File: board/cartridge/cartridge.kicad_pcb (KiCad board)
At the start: 4 copper layers, 58.4 x 56 mm, 42 parts, among them J1 TF-115-BCP9, J2 HC-TYPE-C-16P-01B, P1 Card Edge, SW1 K3-1410S, SW2 K3-1410S, U1 AMS1117-3.3, U2 ESP32-S3-WROOM-1U, U3 TUSB320, U4 TXS0108E, U5 74LVC245, U6 74LVT14, U7 74LVC541, U8 74LVC541, U9 PCM5100

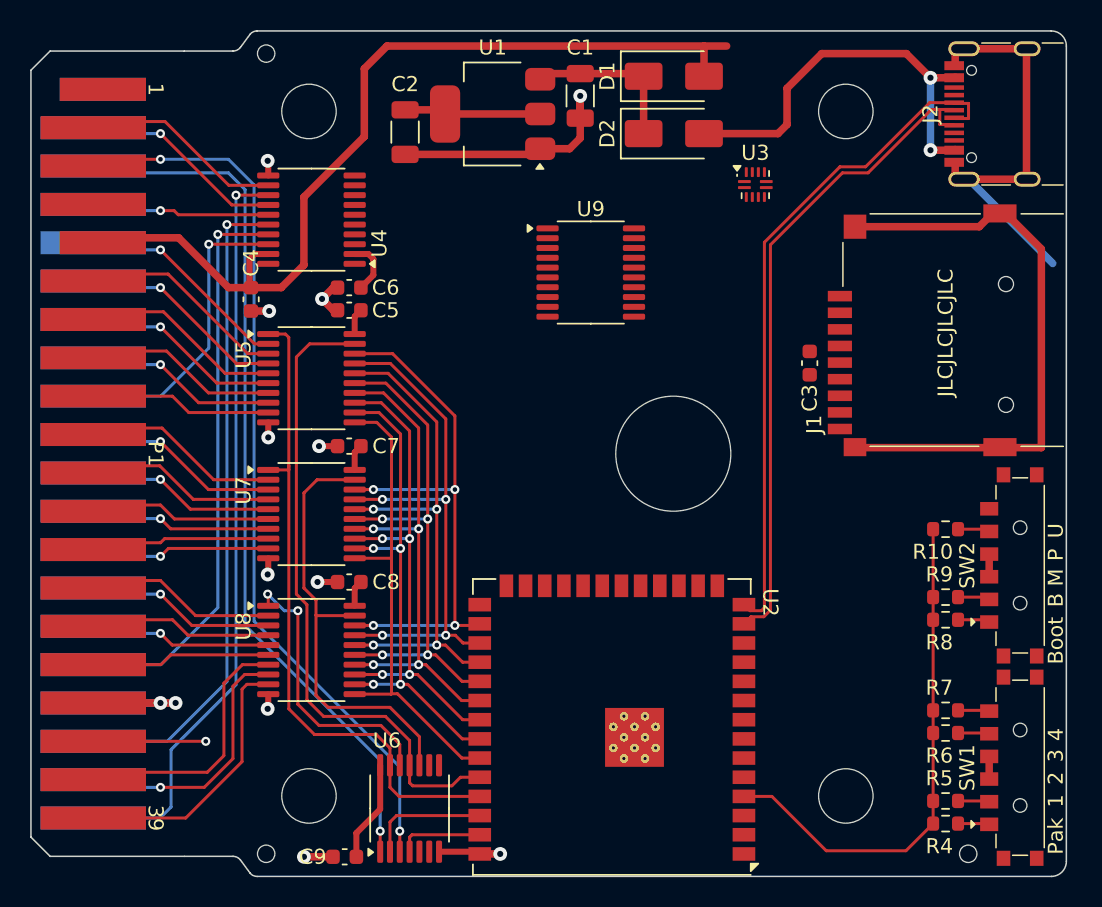
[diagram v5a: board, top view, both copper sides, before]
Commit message: Fully route 5V signals.
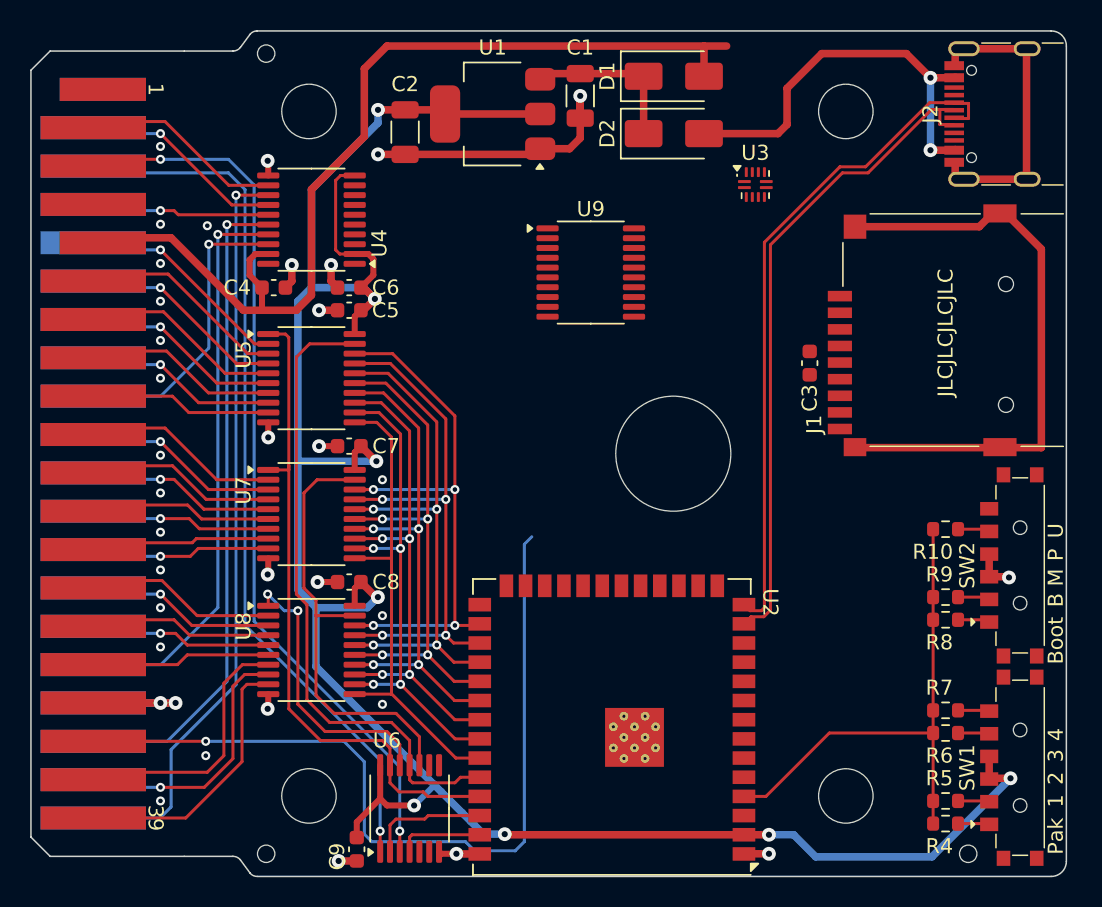
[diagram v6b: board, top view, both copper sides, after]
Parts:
- moved C4 1.69 mm to (127.5, 89.0), turned to 0 degrees
- moved C9 0.94 mm to (133.0, 126.2), turned to -90 degrees
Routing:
- net +3V3: track 26.1 -> 152.5 mm, vias 0 -> 8
- net /Host/SND: track 7.45 -> 55.0 mm
- net +5V: track 60.0 -> 64.5 mm
- net GND: track 112.6 -> 108.8 mm, vias 13 -> 35

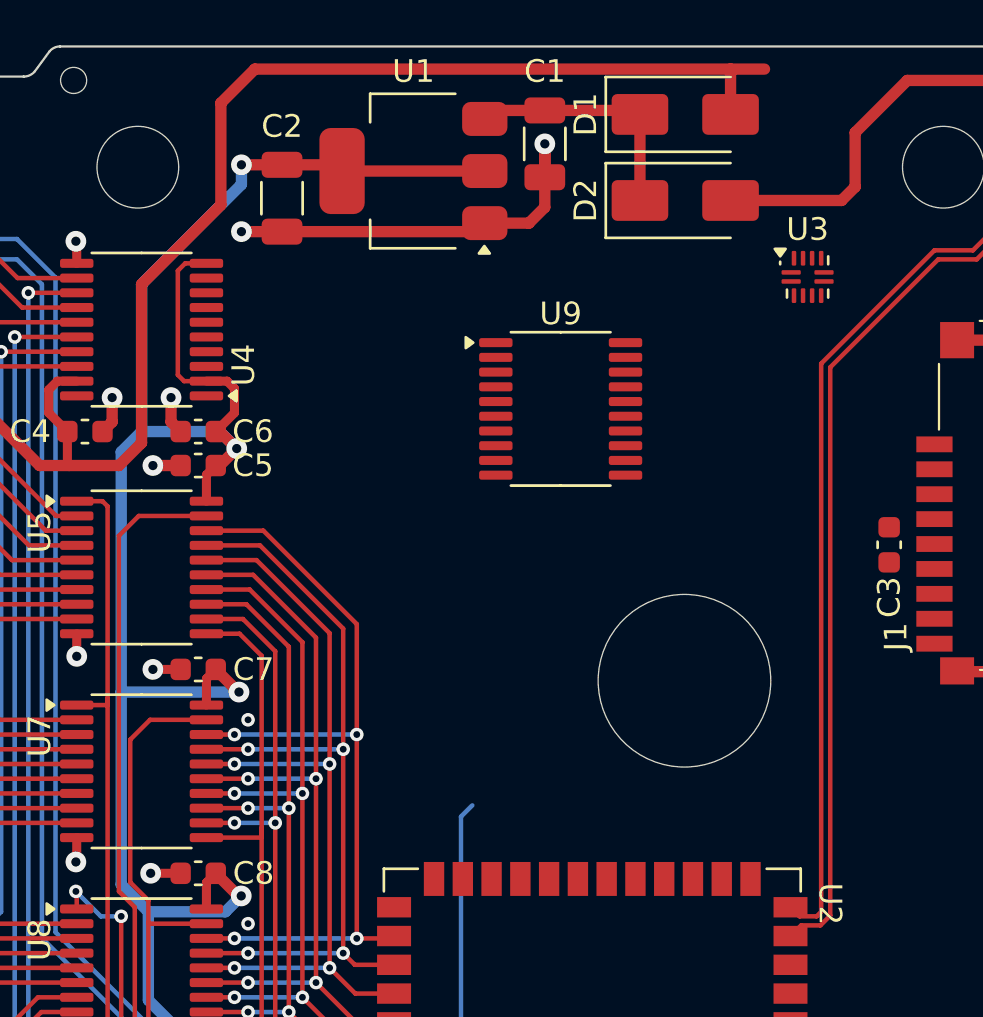
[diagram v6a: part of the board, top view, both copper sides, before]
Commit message: Attach control bus to MCU.
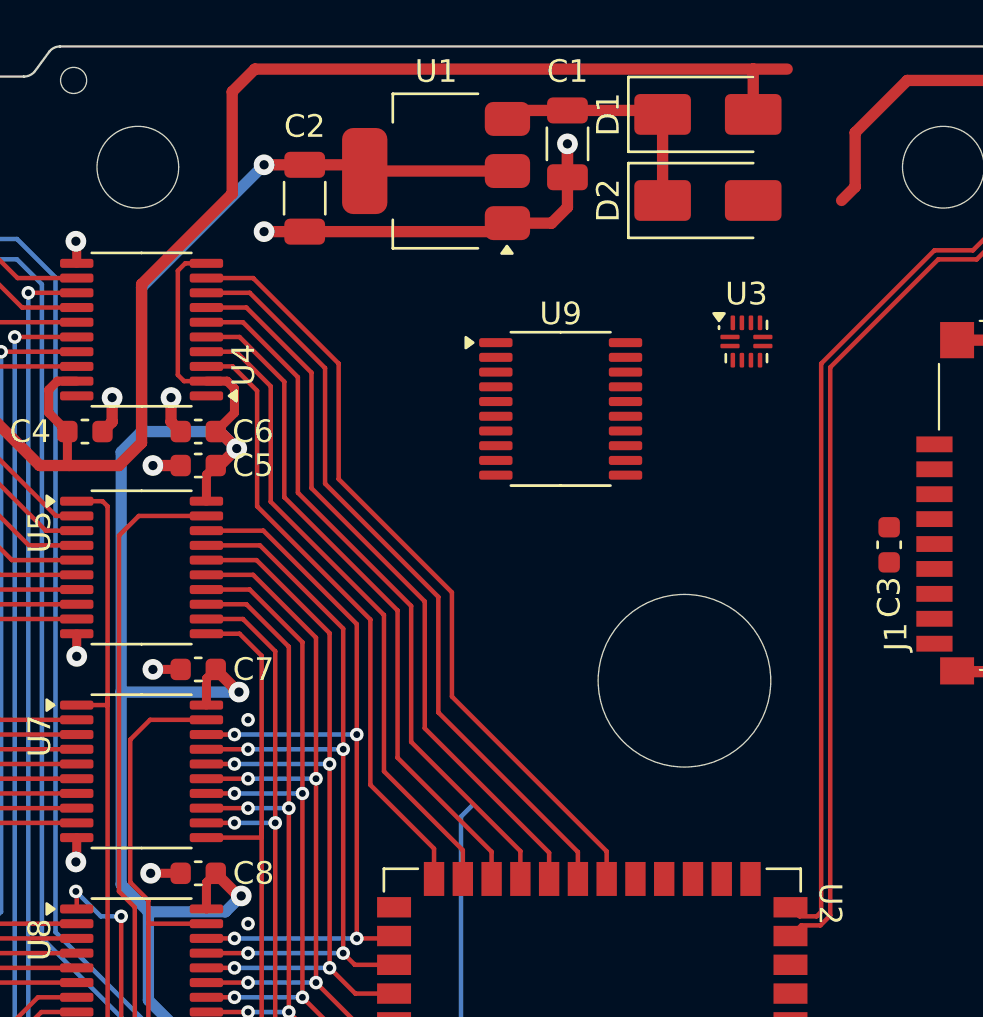
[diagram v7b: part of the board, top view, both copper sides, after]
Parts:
- moved U3 3.93 mm to (156.7, 85.0)
- moved C1 1.00 mm to (148.8, 76.3)
- moved C2 1.00 mm to (137.2, 78.7)
- moved D1 1.00 mm to (155.0, 75.0)
- moved D2 1.00 mm to (155.0, 78.8)
- moved U1 1.00 mm to (143.0, 77.5)
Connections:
- P1 pad 18: /Host/R/~{W} -> /Host/R/~{W}_5
- P1 pad 3: /Host/~{HALT} -> /Host/~{HALT}_5
- P1 pad 32: /Host/~{CTS} -> /Host/~{CTS}_5
- P1 pad 36: /Host/~{SCS} -> /Host/~{SCS}_5
- P1 pad 4: /Host/~{NMI} -> /Host/~{NMI}_5
- P1 pad 40: /Host/~{SLENB} -> /Host/~{SLENB}_5
- P1 pad 8: /Host/~{CART} -> /Host/~{CART}_5
- U2 pad 20: unconnected-(U2-GPIO12-Pad20) -> /~{HALT}
- U2 pad 21: unconnected-(U2-GPIO13-Pad21) -> /~{SLENB}
- U2 pad 22: unconnected-(U2-GPIO14-Pad22) -> /~{NMI}
- U2 pad 23: unconnected-(U2-GPIO21-Pad23) -> /~{CART}
- U2 pad 24: /IN_H/~{OUT_L} -> /~{SCS}
- U2 pad 25: unconnected-(U2-GPIO48-Pad25) -> /~{CTS}
- U2 pad 26: unconnected-(U2-GPIO45-Pad26) -> /R/~{W}
- U4 pad 12: /Host/~{HALT} -> /Host/~{HALT}_5
- U4 pad 13: /Host/~{SLENB} -> /Host/~{SLENB}_5
- U4 pad 14: /Host/~{NMI} -> /Host/~{NMI}_5
- U4 pad 15: /Host/~{CART} -> /Host/~{CART}_5
- U4 pad 16: /Host/~{SCS} -> /Host/~{SCS}_5
- U4 pad 17: /Host/~{CTS} -> /Host/~{CTS}_5
- U4 pad 18: /Host/R/~{W} -> /Host/R/~{W}_5
- U4 pad 3: /Host/R/~{W} -> /R/~{W}
- U4 pad 4: /Host/~{CTS} -> /~{CTS}
- U4 pad 5: /Host/~{SCS} -> /~{SCS}
- U4 pad 6: /Host/~{CART} -> /~{CART}
- U4 pad 7: /Host/~{NMI} -> /~{NMI}
- U4 pad 8: /Host/~{SLENB} -> /~{SLENB}
- U4 pad 9: /Host/~{HALT} -> /~{HALT}
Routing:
- net /Host/~{SLENB}_5: track 0.00 -> 49.9 mm, vias 0 -> 1
- net /Host/~{SLENB}: track 49.9 -> 0.00 mm, vias 1 -> 0
- net /Host/~{SCS}_5: track 0.00 -> 43.5 mm, vias 0 -> 1
- net /Host/~{SCS}: track 43.5 -> 0.00 mm, vias 1 -> 0
- net /Host/~{CTS}_5: track 0.00 -> 37.9 mm, vias 0 -> 1
- net /Host/~{CTS}: track 37.9 -> 0.00 mm, vias 1 -> 0
- net /~{HALT}: track 0.00 -> 35.1 mm
- net /~{SLENB}: track 0.00 -> 33.8 mm
- net /~{NMI}: track 0.00 -> 32.5 mm
- net /~{CART}: track 0.00 -> 31.3 mm
- net /~{SCS}: track 0.00 -> 30.0 mm
- net /~{CTS}: track 0.00 -> 28.7 mm
- net /R/~{W}: track 0.00 -> 27.5 mm
- net /Host/R/~{W}_5: track 0.00 -> 19.8 mm, vias 0 -> 1
- net /Host/R/~{W}: track 19.8 -> 0.00 mm, vias 1 -> 0
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
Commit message: More bus routing.
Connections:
- U2 pad 18: unconnected-(U2-GPIO10-Pad18) -> /~{HALT}
- U2 pad 19: unconnected-(U2-GPIO11-Pad19) -> /~{SLENB}
- U2 pad 20: /~{HALT} -> /~{NMI}
- U2 pad 21: /~{SLENB} -> /~{CART}
- U2 pad 22: /~{NMI} -> /~{SCS}
- U2 pad 23: /~{CART} -> /~{CTS}
- U2 pad 24: /~{SCS} -> /R/~{W}
- U2 pad 25: /~{CTS} -> unconnected-(U2-GPIO48-Pad25)
- U2 pad 26: /R/~{W} -> unconnected-(U2-GPIO45-Pad26)
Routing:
- net /~{SCS}: track 30.0 -> 31.0 mm
- net /~{CART}: track 31.3 -> 32.3 mm
- net /R/~{W}: track 27.5 -> 28.5 mm
- net /~{SLENB}: track 33.8 -> 34.8 mm
- net /~{NMI}: track 32.5 -> 33.6 mm
- net /~{HALT}: track 35.1 -> 36.1 mm
- net /~{CTS}: track 28.7 -> 29.8 mm
